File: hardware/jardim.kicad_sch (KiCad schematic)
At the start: 79 parts, among them J1 DC_INPUT, J10 DHT22_AMB, J11 LIGHT_SENSOR_1, J12 LIGHT_SENSOR_2, J13 LEVEL_SENSOR_1, J14 LEVEL_SENSOR_2, J15 SOIL_HUMIDITY_SENSOR_1, J16 SOIL_HUMIDITY_SENSOR_2, J17 USB_A, J18 USB_C_Receptacle_PowerOnly_6P, J2 PUMP_1, J3 PUMP_2, J4 LIGHT_1, J5 LIGHG_2, J6 HEAT_1, J7 HEAT_2, J8 DS12B20_2, J9 DS18B20_1, Q1 FQP30N06L, Q2 FQP30N06L, Q3 FQP30N06L, Q4 FQP30N06L, Q5 FQP30N06L, Q6 FQP30N06L, Q7 BC337, SW1 SW_Push, SW2 SW_Push, SW3 SW_Push, SW4 SW_SPST, U1 AM2302, U2 DM-OLED096-636

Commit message: lemure e usb c
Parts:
- removed J17: USB_A, symbol Connector:USB_A
- added R22, R23: 5.1k, Resistor_THT:R_Axial_DIN0207_L6.3mm_D2.5mm_P10.16mm_Horizontal, symbol Device:R
- J18: footprint (none) -> Connector_USB:USB_C_Receptacle_GCT_USB4125-xx-x_6P_TopMnt_Horizontal
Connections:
- net +5V: now also J18.A9 (VBUS), J18.B9 (VBUS)
- net GND: now also J18.A12 (GND), J18.B12 (GND), J18.SH (SHIELD), R22.1, R23.2
- net at J18.A5 (CC1): now also R22.2
- net at J18.B5 (CC2): now also R23.1

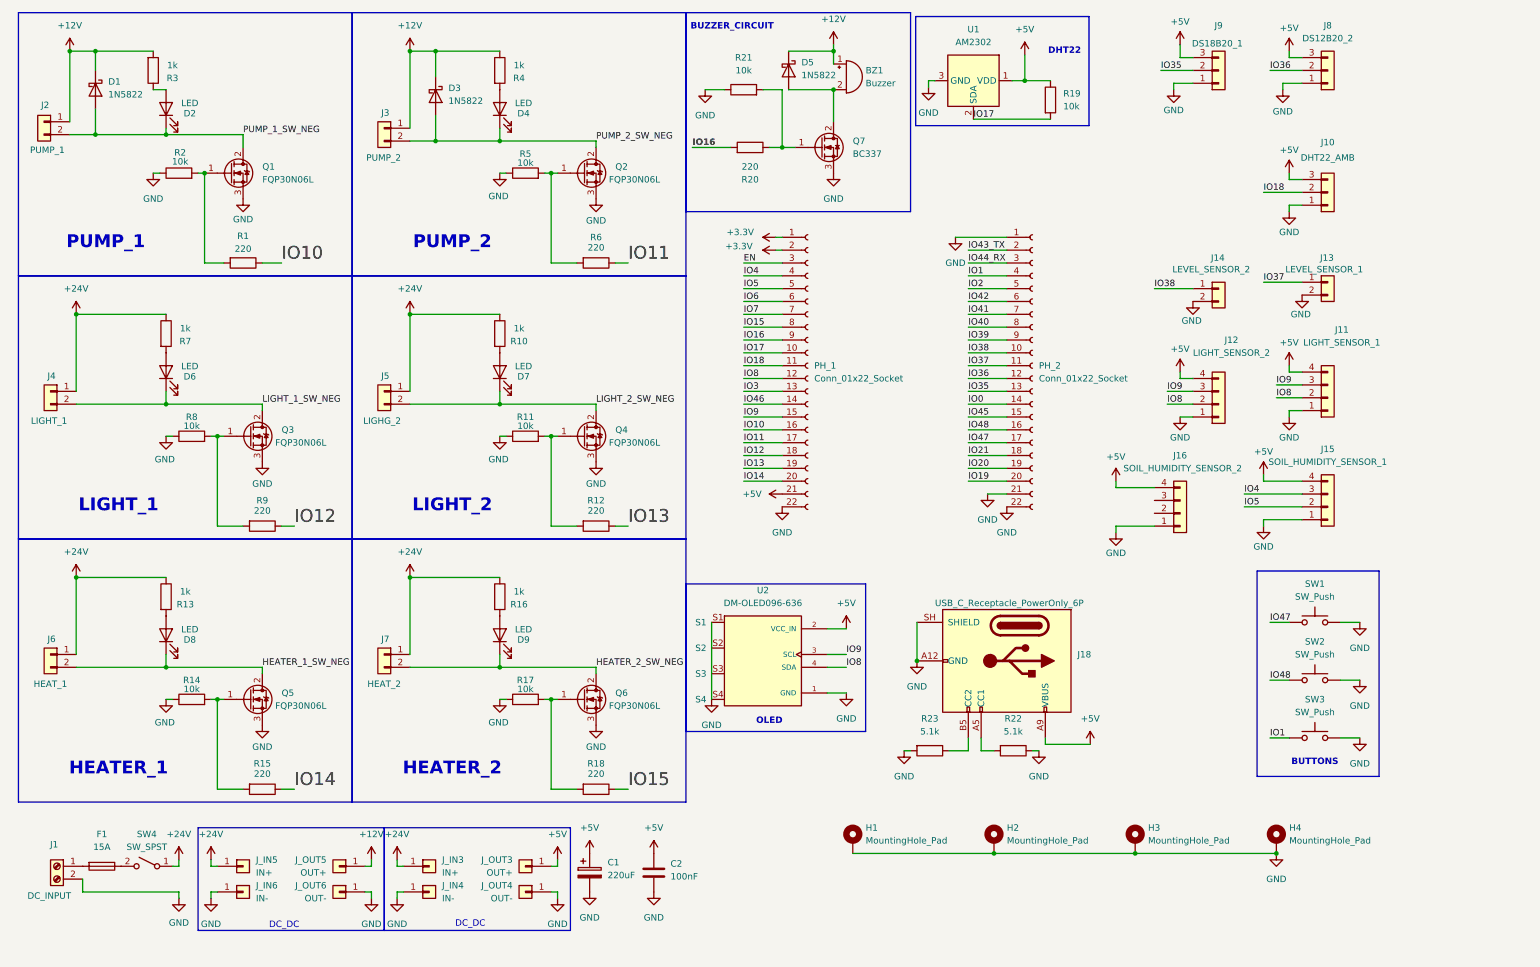
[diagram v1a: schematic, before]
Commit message: pull up sensores, debaunce botoes
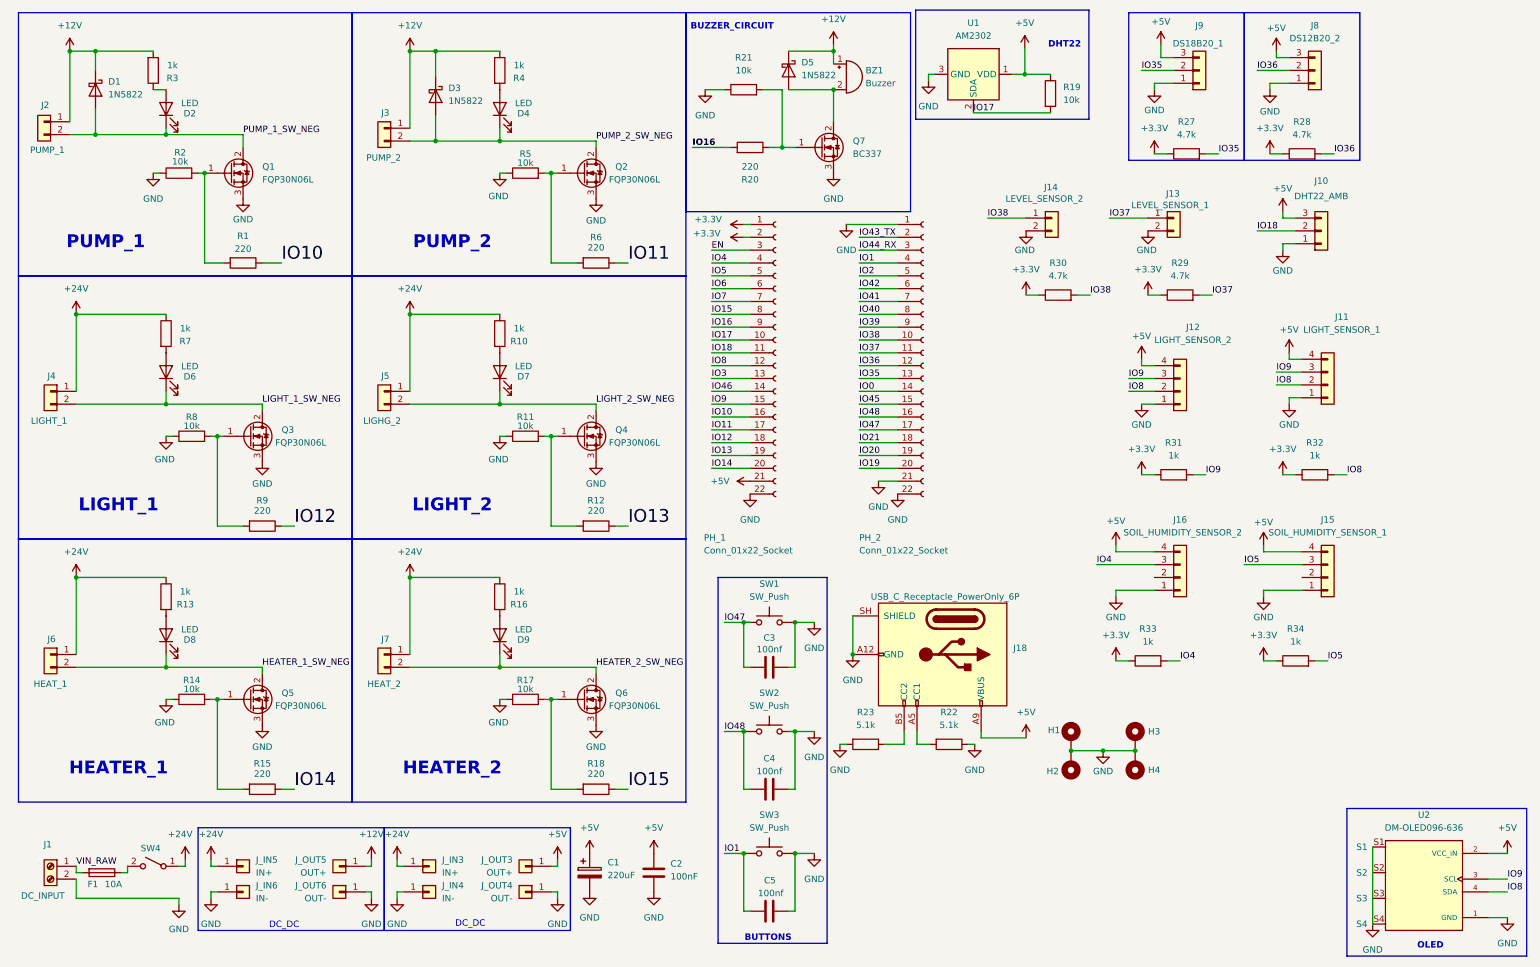
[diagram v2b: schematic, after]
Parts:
- added C3, C4, C5: 100nf, Capacitor_THT:C_Disc_D3.0mm_W1.6mm_P2.50mm, symbol Device:C
- added R27, R28, R29, R30: 4.7k, Resistor_THT:R_Axial_DIN0207_L6.3mm_D2.5mm_P7.62mm_Horizontal, symbol Device:R
- added R31, R32, R33, R34: 1k, Resistor_THT:R_Axial_DIN0207_L6.3mm_D2.5mm_P7.62mm_Horizontal, symbol Device:R
- F1: value 15A -> 10A
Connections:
- net +3.3V: now also R27.1, R28.1, R29.1, R30.1, R31.1, R32.1, R33.1, R34.1
- net GND: now also C3.1, C4.1, C5.1
- net IO1: now also C5.2
- net IO35: now also R27.2
- net IO36: now also R28.2
- net IO37: now also R29.2
- net IO38: now also R30.2
- net IO4: now also J16.3 (Pin_3), R33.2; no longer J15.3 (Pin_3)
- net IO47: now also C3.2
- net IO48: now also C4.2
- net IO5: now also J15.3 (Pin_3), R34.2; no longer J15.2 (Pin_2)
- net IO8: now also R32.2
- net IO9: now also R31.2
- net VIN_RAW: now reaches F1.2, J1.1 (Pin_1)
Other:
- moved on the sheet: F1, H1, H2, H3, H4, J1, J10, J11, J12, J13, J14, J15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

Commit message: ajustes
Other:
- moved on the sheet: H1, H2, H3, H4, J18, PH_1, PH_2, R22, R23, U2

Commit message: sem avisos, pronto para rotear
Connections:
- net VIN_AFTER_FUSE: now reaches F1.1, SW4.2 (B)
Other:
- moved on the sheet: R19, U1
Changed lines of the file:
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@@
 	)
 	(rectangle
-		(start 190.246 12.192)
-		(end 224.536 33.782)
+		(start 189.23 12.7)
+		(end 224.536 35.052)
 		(stroke
 			(width 0)
@@
 	(text "DHT22"
 		(exclude_from_sim no)
-		(at 219.71 19.05 0)
+		(at 219.71 20.32 0)
 		(effects
 			(font
@@
 	)
 	(junction
+		(at 33.02 182.88)
+		(diameter 0)
+		(color 0 0 0 0)
+	)
+	(junction
 		(at 173.99 20.32)
 		(diameter 0)
@@
 	)
 	(junction
-		(at 211.836 24.892)
+		(at 211.836 26.162)
 		(diameter 0)
 		(color 0 0 0 0)
@@
 	(wire
 		(pts
-			(xy 34.29 182.88) (xy 33.02 182.88)
-		)
-		(stroke
-			(width 0)
-			(type default)
-		)
-	)
-	(wire
-		(pts
 			(xy 27.94 20.32) (xy 27.94 24.13)
 		)
@@
 	(wire
 		(pts
-			(xy 194.056 24.892) (xy 192.786 24.892)
+			(xy 194.056 26.162) (xy 192.786 26.162)
 		)
 		(stroke
@@
 	(wire
 		(pts
+			(xy 33.02 182.88) (xy 34.29 181.61)
+		)
+		(stroke
+			(width 0)
+			(type default)
+		)
+	)
+	(wire
+		(pts
 			(xy 264.16 81.28) (xy 266.7 81.28)
 		)
@@
 	(wire
 		(pts
-			(xy 192.786 24.892) (xy 192.786 26.162)
+			(xy 192.786 26.162) (xy 192.786 27.432)
 		)
 		(stroke
@@
 	(wire
 		(pts
-			(xy 211.836 19.812) (xy 211.836 24.892)
+			(xy 211.836 21.082) (xy 211.836 26.162)
 		)
 		(stroke
@@
 	(wire
 		(pts
-			(xy 201.676 32.512) (xy 216.916 32.512)
+			(xy 201.676 33.782) (xy 216.916 33.782)
 		)
 		(stroke
@@
 	(wire
 		(pts
+			(xy 30.48 177.8) (xy 33.02 177.8)
+		)
+		(stroke
+			(width 0)
+			(type default)
+		)
+	)
+	(wire
+		(pts
 			(xy 45.72 180.34) (xy 45.72 181.61)
 		)
@@
 	(wire
 		(pts
+			(xy 30.48 176.53) (xy 30.48 177.8)
+		)
+		(stroke
+			(width 0)
+			(type default)
+		)
+	)
+	(wire
+		(pts
 			(xy 90.17 20.32) (xy 90.17 35.56)
 		)
@@
 	(wire
 		(pts
-			(xy 34.29 182.88) (xy 34.29 181.61)
-		)
-		(stroke
-			(width 0)
-			(type default)
-		)
-	)
-	(wire
-		(pts
 			(xy 148.59 87.63) (xy 156.21 87.63)
 		)
@@
 	(wire
 		(pts
+			(xy 33.02 177.8) (xy 33.02 182.88)
+		)
+		(stroke
+			(width 0)
+			(type default)
+		)
+	)
+	(wire
+		(pts
 			(xy 257.81 24.13) (xy 264.16 24.13)
 		)
@@
 	(wire
 		(pts
-			(xy 209.296 24.892) (xy 211.836 24.892)
+			(xy 209.296 26.162) (xy 211.836 26.162)
 		)
 		(stroke
@@
 	(wire
 		(pts
-			(xy 211.836 24.892) (xy 216.916 24.892)
+			(xy 211.836 26.162) (xy 216.916 26.162)
 		)
 		(stroke
@@
 	)
 	(label "IO17"
-		(at 201.676 32.512 0)
+		(at 201.676 33.782 0)
 		(effects
 			(font
@@
 		(effects
 			(font
-				(size 1.27 1.27)
+				(size 0.635 0.635)
 			)
 			(justify left bottom)
@@
 		)
 	)
+	(label "VIN_AFTER_FUSE"
+		(at 30.48 176.53 0)
+		(effects
+			(font
+				(size 0.635 0.635)
+			)
+			(justify left bottom)
+		)
+	)
 	(label "IO35"
 		(at 250.19 40.64 0)
@@
 	(symbol
 		(lib_id "Sensor:AM2302")
-		(at 201.676 24.892 270)
+		(at 201.676 26.162 270)
 		(unit 1)
 		(body_style 1)
@@
 		(fields_autoplaced yes)
 		(property "Reference" "U1"
-			(at 201.676 14.732 90)
+			(at 201.676 16.002 90)
 			(show_name no)
 			(do_not_autoplace no)
@@
 		)
 		(property "Value" "AM2302"
-			(at 201.676 17.272 90)
+			(at 201.676 18.542 90)
 			(show_name no)
 			(do_not_autoplace no)
@@
 		)
 		(property "Footprint" "Sensor:ASAIR_AM2302_P2.54mm_Vertical"
-			(at 191.516 24.892 0)
+			(at 191.516 26.162 0)
 			(hide yes)
 			(show_name no)
@@
 		)
 		(property "Datasheet" "http://akizukidenshi.com/download/ds/aosong/AM2302.pdf"
-			(at 208.026 28.702 0)
+			(at 208.026 29.972 0)
 			(hide yes)
 			(show_name no)
@@
 		)
 		(property "Description" "3.3 to 5.0V, Temperature and humidity module,  DHT22, AM2302"
-			(at 201.676 24.892 0)
+			(at 201.676 26.162 0)
 			(hide yes)
 			(show_name no)
@@
 	(symbol
 		(lib_id "power:+5V")
-		(at 211.836 19.812 0)
+		(at 211.836 21.082 0)
 		(unit 1)
 		(body_style 1)
@@
 		(fields_autoplaced yes)
 		(property "Reference" "#PWR039"
-			(at 211.836 23.622 0)
+			(at 211.836 24.892 0)
 			(hide yes)
 			(show_name no)
@@
 		)
 		(property "Value" "+5V"
-			(at 211.836 14.732 0)
+			(at 211.836 16.002 0)
 			(show_name no)
 			(do_not_autoplace no)
@@
 		)
 		(property "Footprint" ""
-			(at 211.836 19.812 0)
+			(at 211.836 21.082 0)
 			(hide yes)
 			(show_name no)
@@
 		)
 		(property "Datasheet" ""
-			(at 211.836 19.812 0)
+			(at 211.836 21.082 0)
 			(hide yes)
 			(show_name no)
@@
 		)
 		(property "Description" "Power symbol creates a global label with name \"+5V\""
-			(at 211.836 19.812 0)
+			(at 211.836 21.082 0)
 			(hide yes)
 			(show_name no)
@@
 	(symbol
 		(lib_id "Device:R")
-		(at 216.916 28.702 0)
+		(at 216.916 29.972 0)
 		(unit 1)
 		(body_style 1)
@@
 		(fields_autoplaced yes)
 		(property "Reference" "R19"
-			(at 219.456 27.4319 0)
+			(at 219.456 28.7019 0)
 			(show_name no)
 			(do_not_autoplace no)
@@
 		)
 		(property "Value" "10k"
-			(at 219.456 29.9719 0)
+			(at 219.456 31.2419 0)
 			(show_name no)
 			(do_not_autoplace no)
@@
 		)
 		(property "Footprint" "Resistor_THT:R_Axial_DIN0207_L6.3mm_D2.5mm_P7.62mm_Horizontal"
-			(at 215.138 28.702 90)
+			(at 215.138 29.972 90)
 			(hide yes)
 			(show_name no)
@@
 		)
 		(property "Datasheet" ""
-			(at 216.916 28.702 0)
+			(at 216.916 29.972 0)
 			(hide yes)
 			(show_name no)
@@
 		)
 		(property "Description" "Resistor"
-			(at 216.916 28.702 0)
+			(at 216.916 29.972 0)
 			(hide yes)
 			(show_name no)
@@
 	(symbol
 		(lib_id "power:GND")
-		(at 192.786 26.162 0)
+		(at 192.786 27.432 0)
 		(unit 1)
 		(body_style 1)
@@
 		(fields_autoplaced yes)
 		(property "Reference" "#PWR038"
-			(at 192.786 32.512 0)
+			(at 192.786 33.782 0)
 			(hide yes)
 			(show_name no)
@@
 		)
 		(property "Value" "GND"
-			(at 192.786 31.242 0)
+			(at 192.786 32.512 0)
 			(show_name no)
 			(do_not_autoplace no)
@@
 		)
 		(property "Footprint" ""
-			(at 192.786 26.162 0)
+			(at 192.786 27.432 0)
 			(hide yes)
 			(show_name no)
@@
 		)
 		(property "Datasheet" ""
-			(at 192.786 26.162 0)
+			(at 192.786 27.432 0)
 			(hide yes)
 			(show_name no)
@@
 		)
 		(property "Description" "Power symbol creates a global label with name \"GND\" , ground"
-			(at 192.786 26.162 0)
+			(at 192.786 27.432 0)
 			(hide yes)
 			(show_name no)
@@
 	)
 	(group ""
+		(members "36834f7f-8285-48e7-a18e-6709d078e4f1" "43618f34-a686-4c66-a7ac-3ed4bba3929d"
+			"9b582545-4161-429e-9acc-5a08f32a2e5a"
+		)
+	)
+	(group ""
 		(members "20d06328-826c-48b3-8cdf-d8901b22d23b" "24e0ce1e-2f5c-4474-b50c-ba1d36bf0a1a"
 			"251f320c-7bdf-486d-b8a6-300ae3def773" "702d38d7-4511-4241-94b6-c4c3d68f2b39"
@@
 		)
 	)
-	(group ""
-		(members "36834f7f-8285-48e7-a18e-6709d078e4f1" "43618f34-a686-4c66-a7ac-3ed4bba3929d"
-			"9b582545-4161-429e-9acc-5a08f32a2e5a"
-		)
-	)
